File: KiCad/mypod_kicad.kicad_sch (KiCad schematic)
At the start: 2 parts

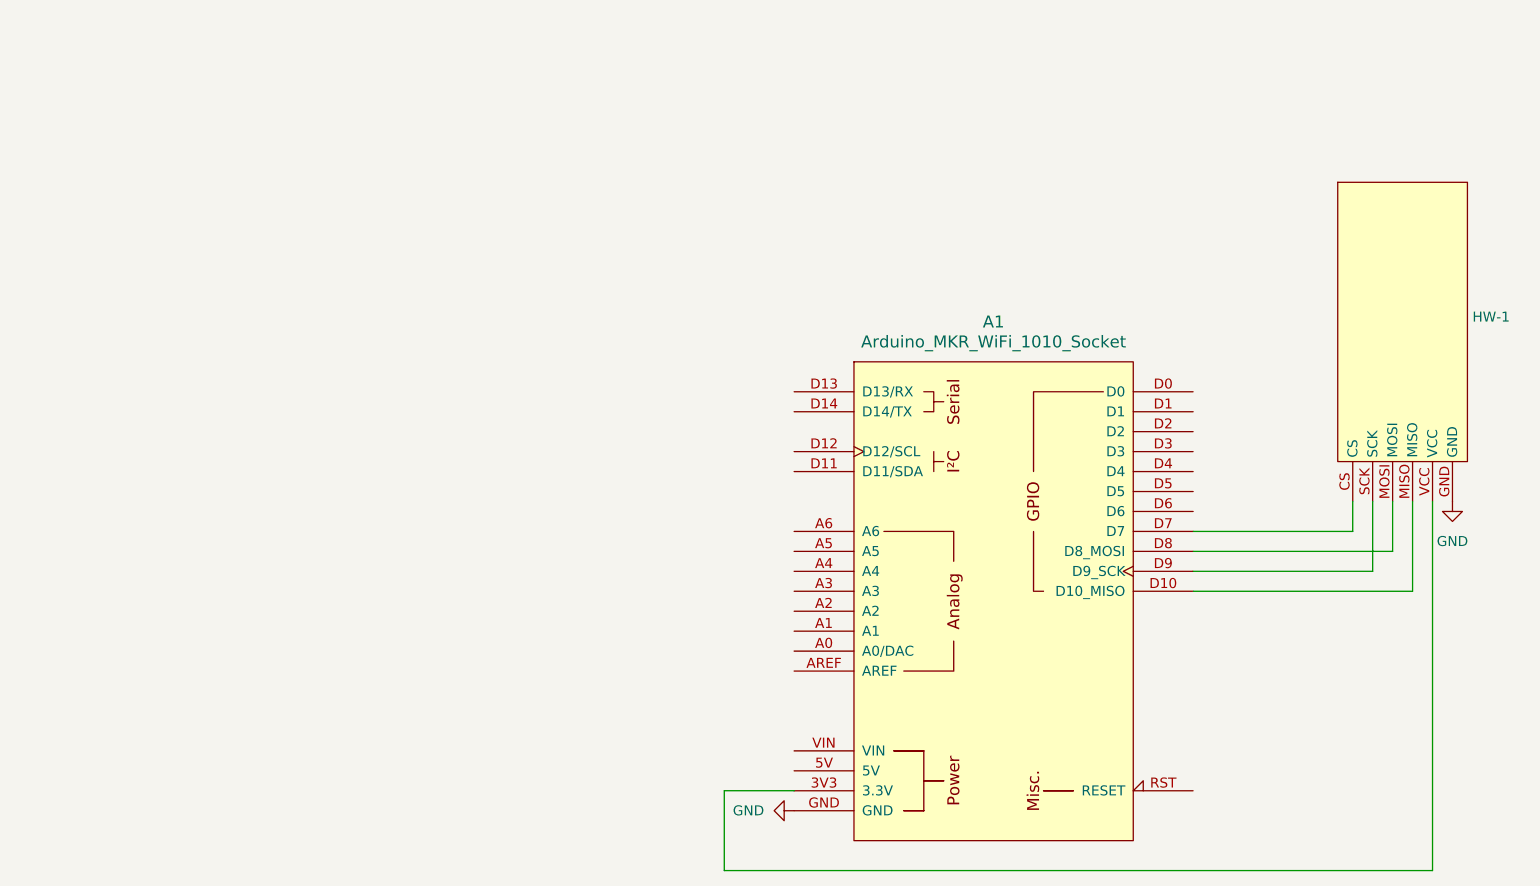
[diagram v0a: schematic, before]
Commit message: Changes: Added indexing of sd Card
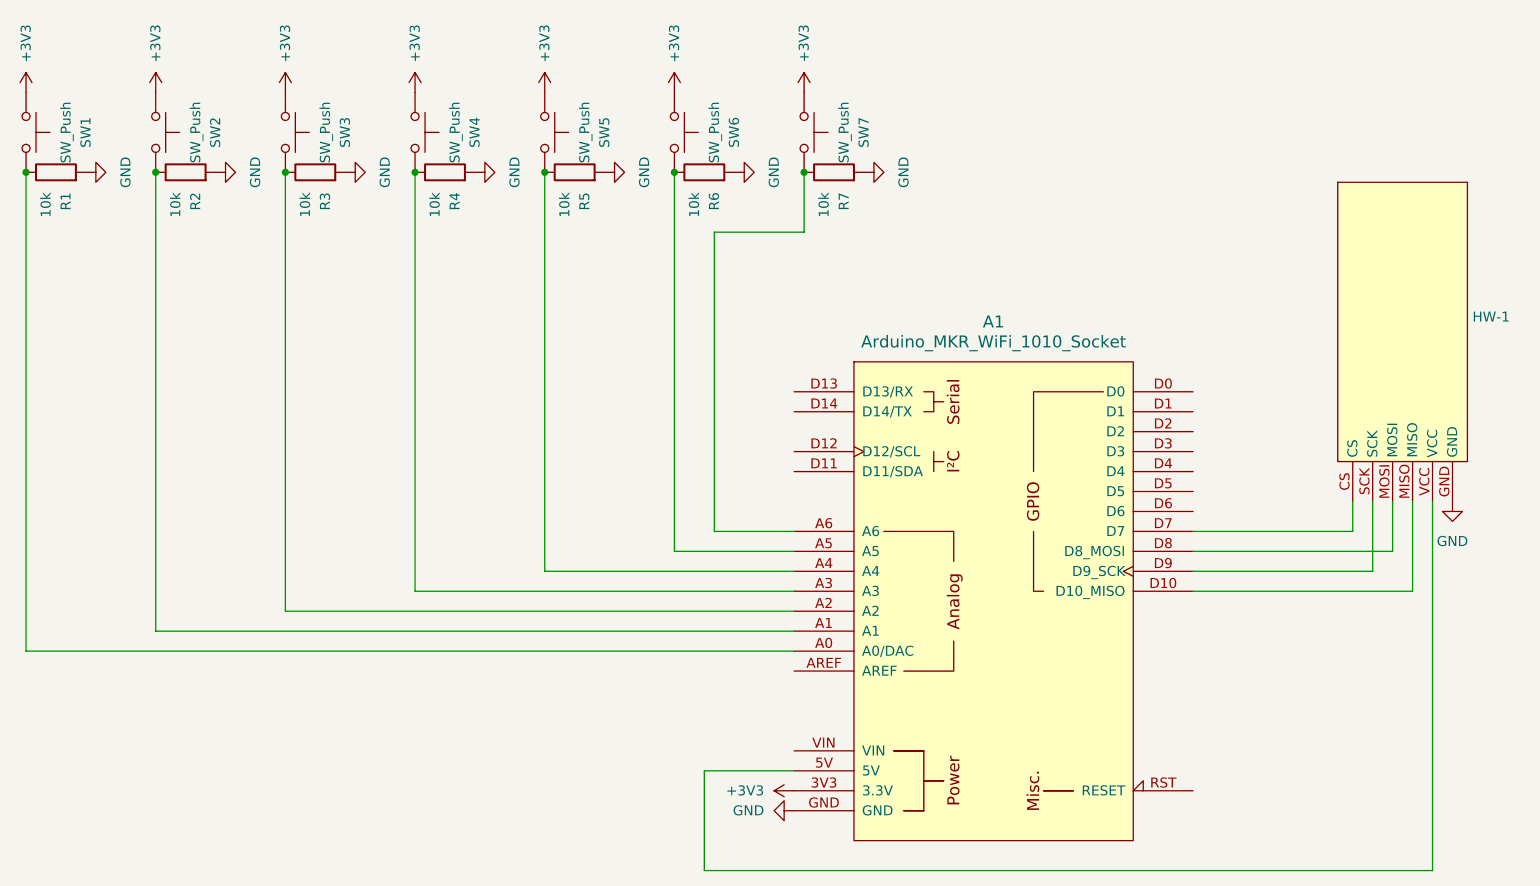
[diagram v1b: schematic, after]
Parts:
- added R1, R2, R3, R4, R5, R6, R7: 10k, symbol Device:R
- added SW1, SW2, SW3, SW4, SW5, SW6, SW7: SW_Push, symbol Switch:SW_Push
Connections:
- net GND: now also R1.2, R2.2, R3.2, R4.2, R5.2, R6.2, R7.2
- net at HW-1.VCC: now also A1.5V; no longer A1.3V3 (3.3V)
- net at A1.A0 (A0/DAC): now also R1.1, SW1.2
- net at A1.A1: now also R2.1, SW2.2
- net at A1.A2: now also R3.1, SW3.2
- net at A1.A3: now also R4.1, SW4.2
- net at A1.A4: now also R5.1, SW5.2
- net at A1.A5: now also R6.1, SW6.2
- net at A1.A6: now also R7.1, SW7.2
- new net +3V3: A1.3V3 (3.3V), SW1.1, SW2.1, SW3.1, SW4.1, SW5.1, SW6.1, SW7.1
